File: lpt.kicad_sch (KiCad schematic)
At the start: 20 parts, among them J6 DB25 FEMALE, K1 TE_OJS_5V_10A, Q3 BC857, U2 74HC245, U3 74HC245, U4 LM358EDR2G, U5 ACSL-6400, U7 ACSL-6400

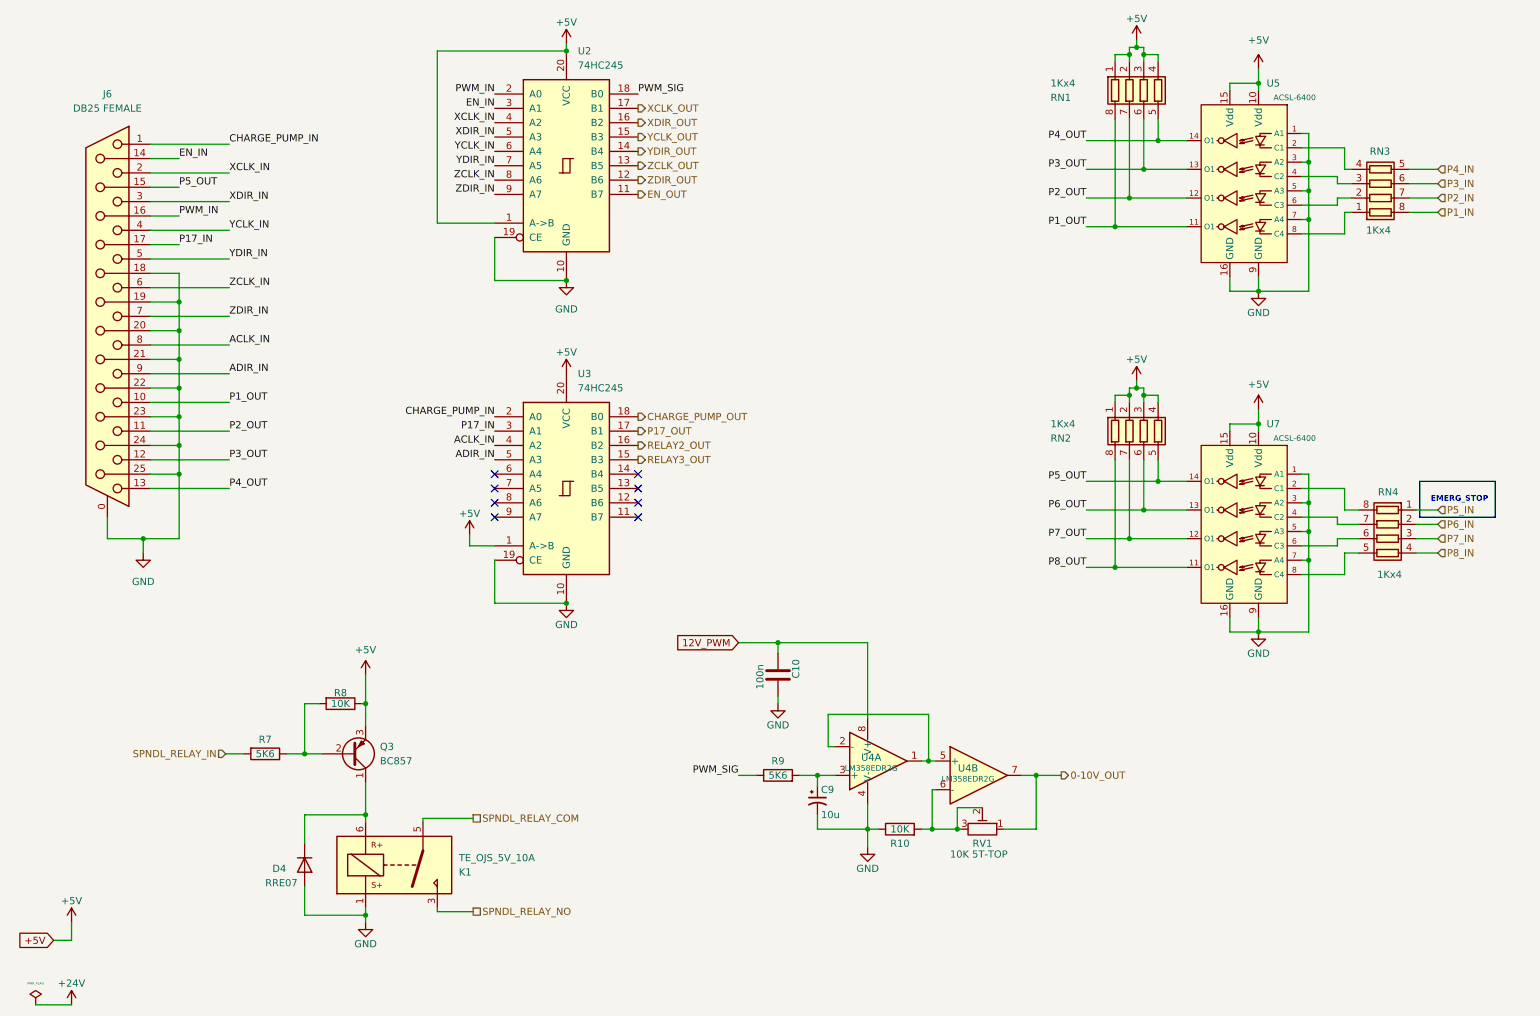
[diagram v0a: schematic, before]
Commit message: Some more decoupling caps and routing optimizations.
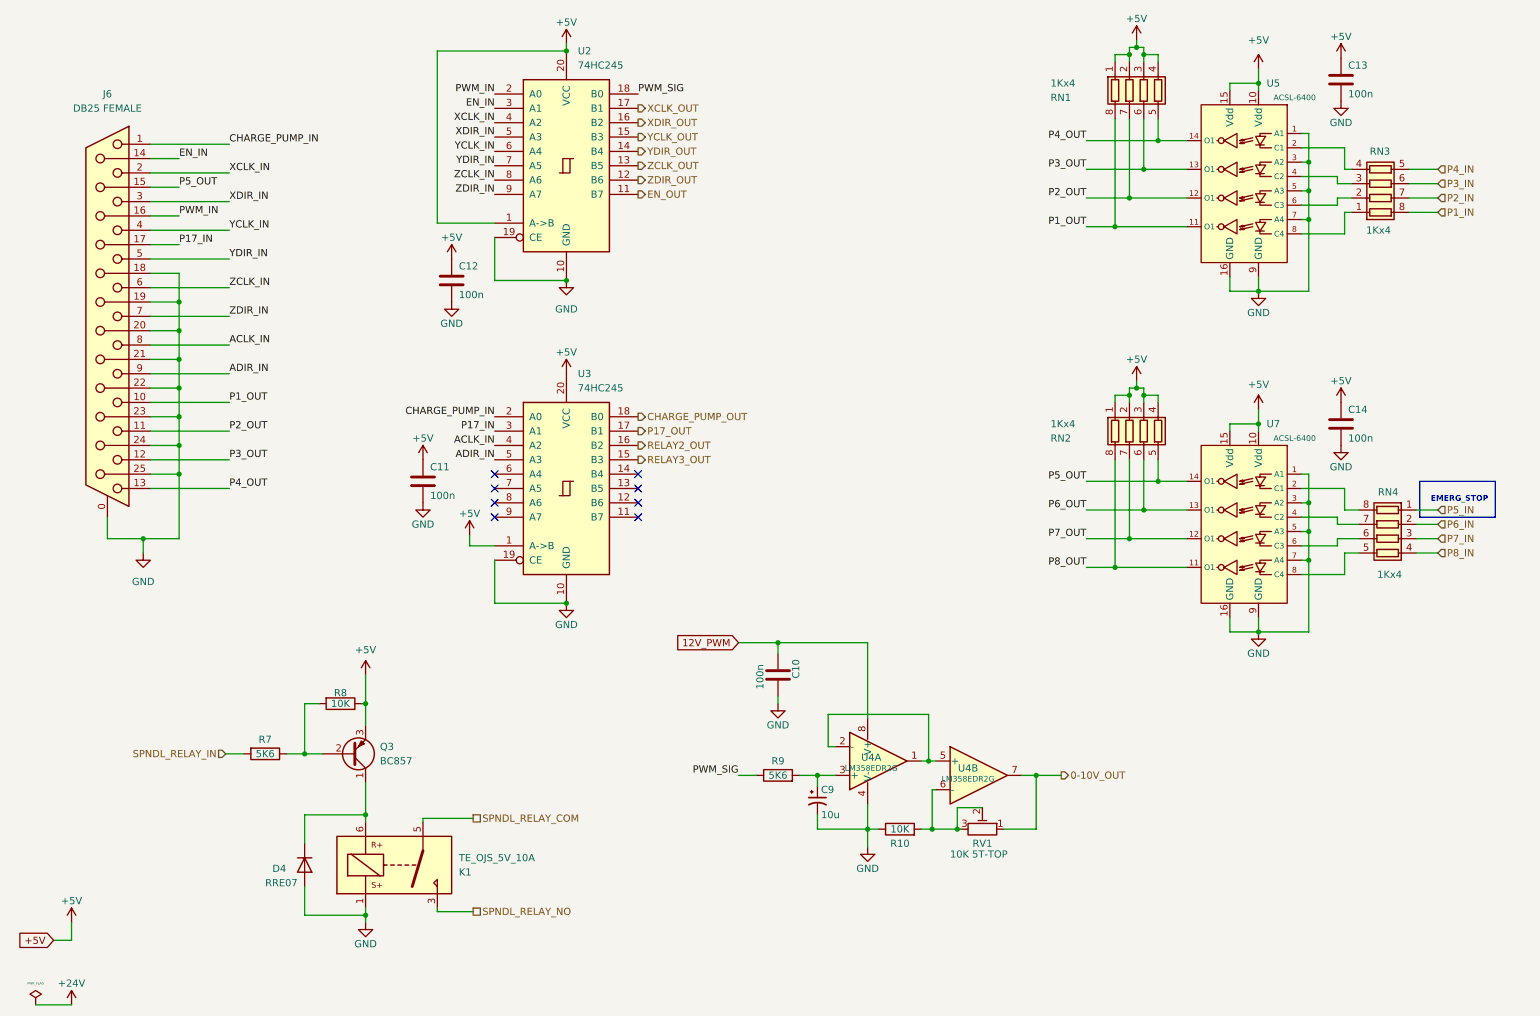
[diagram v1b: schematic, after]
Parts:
- added C11, C12, C13, C14: 100n, Capacitor_SMD:C_0603_1608Metric, symbol Device:C
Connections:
- net +5V: now also C11.1, C12.1, C13.1, C14.1
- net GND: now also C11.2, C12.2, C13.2, C14.2
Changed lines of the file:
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@@
     (effects (font (size 1.27 1.27)) (justify left))
+  )
+  (symbol (lib_id "power:+5V") (at 92.71 58.42 0) (unit 1)
+    (in_bom yes) (on_board yes)
+    (property "Reference" "#PWR041" (id 0) (at 92.71 62.23 0)
+      (effects (font (size 1.27 1.27)) hide)
+    )
+    (property "Value" "+5V" (id 1) (at 92.71 54.61 0))
+    (property "Footprint" "" (id 2) (at 92.71 58.42 0)
+      (effects (font (size 1.27 1.27)) hide)
+    )
+    (property "Datasheet" "" (id 3) (at 92.71 58.42 0)
+      (effects (font (size 1.27 1.27)) hide)
+    )
+    (pin "1")
   )
   (symbol (lib_id "power:PWR_FLAG") (at 19.05 190.5 0) (unit 1)
@@
     (pin "7")
     (pin "8")
+  )
+  (symbol (lib_id "power:GND") (at 92.71 66.04 0) (unit 1)
+    (in_bom yes) (on_board yes)
+    (property "Reference" "#PWR042" (id 0) (at 92.71 72.39 0)
+      (effects (font (size 1.27 1.27)) hide)
+    )
+    (property "Value" "GND" (id 1) (at 92.71 69.85 0))
+    (property "Footprint" "" (id 2) (at 92.71 66.04 0)
+      (effects (font (size 1.27 1.27)) hide)
+    )
+    (property "Datasheet" "" (id 3) (at 92.71 66.04 0)
+      (effects (font (size 1.27 1.27)) hide)
+    )
+    (pin "1")
+  )
+  (symbol (lib_id "power:GND") (at 250.19 91.44 0) (unit 1)
+    (in_bom yes) (on_board yes)
+    (property "Reference" "#PWR046" (id 0) (at 250.19 97.79 0)
+      (effects (font (size 1.27 1.27)) hide)
+    )
+    (property "Value" "GND" (id 1) (at 250.19 95.25 0))
+    (property "Footprint" "" (id 2) (at 250.19 91.44 0)
+      (effects (font (size 1.27 1.27)) hide)
+    )
+    (property "Datasheet" "" (id 3) (at 250.19 91.44 0)
+      (effects (font (size 1.27 1.27)) hide)
+    )
+    (pin "1")
   )
   (symbol (lib_id "power:GND") (at 113.03 119.38 0) (unit 1)
@@
     (pin "9")
   )
+  (symbol (lib_id "Device:C") (at 92.71 62.23 0) (unit 1)
+    (in_bom yes) (on_board yes)
+    (property "Reference" "C12" (id 0) (at 93.98 59.69 0)
+      (effects (font (size 1.27 1.27)) (justify left))
+    )
+    (property "Value" "100n" (id 1) (at 93.98 64.77 0)
+      (effects (font (size 1.27 1.27)) (justify left))
+    )
+    (property "Footprint" "Capacitor_SMD:C_0603_1608Metric" (id 2) (at 93.6752 66.04 0)
+      (effects (font (size 1.27 1.27)) hide)
+    )
+    (property "Datasheet" "~" (id 3) (at 92.71 62.23 0)
+      (effects (font (size 1.27 1.27)) hide)
+    )
+    (pin "1")
+    (pin "2")
+  )
+  (symbol (lib_id "Device:C") (at 250.19 87.63 0) (unit 1)
+    (in_bom yes) (on_board yes)
+    (property "Reference" "C14" (id 0) (at 251.46 85.09 0)
+      (effects (font (size 1.27 1.27)) (justify left))
+    )
+    (property "Value" "100n" (id 1) (at 251.46 90.17 0)
+      (effects (font (size 1.27 1.27)) (justify left))
+    )
+    (property "Footprint" "Capacitor_SMD:C_0603_1608Metric" (id 2) (at 251.1552 91.44 0)
+      (effects (font (size 1.27 1.27)) hide)
+    )
+    (property "Datasheet" "~" (id 3) (at 250.19 87.63 0)
+      (effects (font (size 1.27 1.27)) hide)
+    )
+    (pin "1")
+    (pin "2")
+  )
   (symbol (lib_id "power:+5V") (at 95.885 107.315 0) (unit 1)
     (in_bom yes) (on_board yes)
@@
     )
     (property "Datasheet" "" (id 3) (at 95.885 107.315 0)
+      (effects (font (size 1.27 1.27)) hide)
+    )
+    (pin "1")
+  )
+  (symbol (lib_id "power:+5V") (at 250.19 22.86 0) (unit 1)
+    (in_bom yes) (on_board yes)
+    (property "Reference" "#PWR043" (id 0) (at 250.19 26.67 0)
+      (effects (font (size 1.27 1.27)) hide)
+    )
+    (property "Value" "+5V" (id 1) (at 250.19 19.05 0))
+    (property "Footprint" "" (id 2) (at 250.19 22.86 0)
+      (effects (font (size 1.27 1.27)) hide)
+    )
+    (property "Datasheet" "" (id 3) (at 250.19 22.86 0)
       (effects (font (size 1.27 1.27)) hide)
     )
@@
     )
     (property "Datasheet" "" (id 3) (at 235.585 24.765 0)
+      (effects (font (size 1.27 1.27)) hide)
+    )
+    (pin "1")
+  )
+  (symbol (lib_id "power:GND") (at 250.19 30.48 0) (unit 1)
+    (in_bom yes) (on_board yes)
+    (property "Reference" "#PWR044" (id 0) (at 250.19 36.83 0)
+      (effects (font (size 1.27 1.27)) hide)
+    )
+    (property "Value" "GND" (id 1) (at 250.19 34.29 0))
+    (property "Footprint" "" (id 2) (at 250.19 30.48 0)
+      (effects (font (size 1.27 1.27)) hide)
+    )
+    (property "Datasheet" "" (id 3) (at 250.19 30.48 0)
       (effects (font (size 1.27 1.27)) hide)
     )
@@
     (pin "7")
     (pin "8")
+  )
+  (symbol (lib_id "Device:C") (at 250.19 26.67 0) (unit 1)
+    (in_bom yes) (on_board yes)
+    (property "Reference" "C13" (id 0) (at 251.46 24.13 0)
+      (effects (font (size 1.27 1.27)) (justify left))
+    )
+    (property "Value" "100n" (id 1) (at 251.46 29.21 0)
+      (effects (font (size 1.27 1.27)) (justify left))
+    )
+    (property "Footprint" "Capacitor_SMD:C_0603_1608Metric" (id 2) (at 251.1552 30.48 0)
+      (effects (font (size 1.27 1.27)) hide)
+    )
+    (property "Datasheet" "~" (id 3) (at 250.19 26.67 0)
+      (effects (font (size 1.27 1.27)) hide)
+    )
+    (pin "1")
+    (pin "2")
   )
   (symbol (lib_id "power:+5V") (at 25.4 175.895 0) (unit 1)
@@
     (pin "2")
   )
+  (symbol (lib_id "power:+5V") (at 250.19 83.82 0) (unit 1)
+    (in_bom yes) (on_board yes)
+    (property "Reference" "#PWR045" (id 0) (at 250.19 87.63 0)
+      (effects (font (size 1.27 1.27)) hide)
+    )
+    (property "Value" "+5V" (id 1) (at 250.19 80.01 0))
+    (property "Footprint" "" (id 2) (at 250.19 83.82 0)
+      (effects (font (size 1.27 1.27)) hide)
+    )
+    (property "Datasheet" "" (id 3) (at 250.19 83.82 0)
+      (effects (font (size 1.27 1.27)) hide)
+    )
+    (pin "1")
+  )
   (symbol (lib_id "power:GND") (at 77.47 175.895 0) (unit 1)
     (in_bom yes) (on_board yes)
@@
     (pin "2")
   )
+  (symbol (lib_id "power:+5V") (at 87.63 93.98 0) (unit 1)
+    (in_bom yes) (on_board yes)
+    (property "Reference" "#PWR039" (id 0) (at 87.63 97.79 0)
+      (effects (font (size 1.27 1.27)) hide)
+    )
+    (property "Value" "+5V" (id 1) (at 87.63 90.17 0))
+    (property "Footprint" "" (id 2) (at 87.63 93.98 0)
+      (effects (font (size 1.27 1.27)) hide)
+    )
+    (property "Datasheet" "" (id 3) (at 87.63 93.98 0)
+      (effects (font (size 1.27 1.27)) hide)
+    )
+    (pin "1")
+  )
   (symbol (lib_id "power:GND") (at 235.585 64.135 0) (unit 1)
     (in_bom yes) (on_board yes)
@@
     (pin "1")
   )
+  (symbol (lib_id "power:GND") (at 87.63 101.6 0) (unit 1)
+    (in_bom yes) (on_board yes)
+    (property "Reference" "#PWR040" (id 0) (at 87.63 107.95 0)
+      (effects (font (size 1.27 1.27)) hide)
+    )
+    (property "Value" "GND" (id 1) (at 87.63 105.41 0))
+    (property "Footprint" "" (id 2) (at 87.63 101.6 0)
+      (effects (font (size 1.27 1.27)) hide)
+    )
+    (property "Datasheet" "" (id 3) (at 87.63 101.6 0)
+      (effects (font (size 1.27 1.27)) hide)
+    )
+    (pin "1")
+  )
   (symbol (lib_id "power:GND") (at 235.585 124.46 0) (unit 1)
     (in_bom yes) (on_board yes)
@@
     (pin "1")
   )
+  (symbol (lib_id "Device:C") (at 87.63 97.79 0) (unit 1)
+    (in_bom yes) (on_board yes)
+    (property "Reference" "C11" (id 0) (at 88.9 95.25 0)
+      (effects (font (size 1.27 1.27)) (justify left))
+    )
+    (property "Value" "100n" (id 1) (at 88.9 100.33 0)
+      (effects (font (size 1.27 1.27)) (justify left))
+    )
+    (property "Footprint" "Capacitor_SMD:C_0603_1608Metric" (id 2) (at 88.5952 101.6 0)
+      (effects (font (size 1.27 1.27)) hide)
+    )
+    (property "Datasheet" "~" (id 3) (at 87.63 97.79 0)
+      (effects (font (size 1.27 1.27)) hide)
+    )
+    (pin "1")
+    (pin "2")
+  )
   (symbol (lib_id "Relay:ADW11") (at 82.55 165.735 0) (mirror x) (unit 1)

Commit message: Lots of changes and errors fixed. Updated vanity images.
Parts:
- added R11: 100, Resistor_SMD:R_0603_1608Metric, symbol Device:R
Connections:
- net ACLK_IN is gone; now on net P8_IN: J6.8, U3.4 (A2)
- net CHARGE_PUMP_IN is gone; now on net P1_IN: J6.1, U3.2 (A0)
- net CHARGE_PUMP_OUT is gone; now on net P1_OUT: U3.18 (B0)
- net EN_OUT is gone; now on net P7_OUT: U2.11 (B7)
- net RELAY2_OUT is gone; now on net P8_OUT: U3.16 (B2)
- net XCLK_IN is gone; now on net P2_IN: J6.2, U2.4 (A2)
- net XDIR_IN is gone; now on net P3_IN: J6.3, U2.5 (A3)
- net XDIR_OUT is gone; now on net P2_OUT: U2.16 (B2)
- net YCLK_IN is gone; now on net P4_IN: J6.4, U2.6 (A4)
- net YCLK_OUT is gone; now on net P3_OUT: U2.15 (B3)
- net YDIR_IN is gone; now on net P5_IN: J6.5, U2.7 (A5)
- net YDIR_OUT is gone; now on net P4_OUT: U2.14 (B4)
- net ZCLK_IN is gone; now on net P6_IN: J6.6, U2.8 (A6)
- net ZCLK_OUT is gone; now on net P5_OUT: U2.13 (B5)
- net ZDIR_IN is gone; now on net P7_IN: J6.7, U2.9 (A7)
- net ZDIR_OUT is gone; now on net P6_OUT: U2.12 (B6)
- net 12V_PWM: now also R11.1; no longer C10.1, U4.8 (V+)
- net P1_IN: no longer RN3.8 (R1.2)
- net P1_OUT: no longer J6.10, RN1.8 (R1.2), U5.11 (O1)
- net P2_IN: no longer RN3.7 (R2.2)
- net P2_OUT: no longer J6.11, RN1.7 (R2.2), U5.12 (O1)
- net P3_IN: no longer RN3.6 (R3.2)
- net P3_OUT: no longer J6.12, RN1.6 (R3.2), U5.13 (O1)
- net P4_IN: no longer RN3.5 (R4.2)
- net P4_OUT: no longer J6.13, RN1.5 (R4.2), U5.14 (O1)
- net P5_IN: no longer RN4.1 (R1.1)
- net P5_OUT: no longer J6.15 (P15), RN2.5 (R4.2), U7.14 (O1)
- net P6_IN: no longer RN4.2 (R2.1)
- net P6_OUT: no longer RN2.6 (R3.2), U7.13 (O1)
- net P7_IN: no longer RN4.3 (R3.1)
- net P7_OUT: no longer RN2.7 (R2.2), U7.12 (O1)
- net P8_IN: no longer RN4.4 (R4.1)
- net P8_OUT: no longer RN2.8 (R1.2), U7.11 (O1)
- net PWM_IN: now also R9.2; no longer J6.16 (P16), U2.2 (A0)
- net at C9.1, U4.3 (+): now also R9.1; no longer R9.2
- net ADIR_IN renamed P9_IN
- net EN_IN renamed P14_IN
- net PWM_SIG renamed P16_OUT
- net P16_OUT: no longer R9.1
- net RELAY3_OUT renamed P9_OUT
- net XCLK_OUT renamed P14_OUT
- new net: C10.1, R11.2, U4.8 (V+)
- new net: RN2.6 (R3.2), U7.13 (O1)
- new net: RN2.7 (R2.2), U7.12 (O1)
- new net: RN2.8 (R1.2), U7.11 (O1)
- new net P10_IN: RN3.8 (R1.2)
- new net P10_OUT: J6.10, RN1.8 (R1.2), U5.11 (O1)
- new net P11_IN: RN3.7 (R2.2)
- new net P11_OUT: J6.11, RN1.7 (R2.2), U5.12 (O1)
- new net P12_IN: RN3.6 (R3.2)
- new net P12_OUT: J6.12, RN1.6 (R3.2), U5.13 (O1)
- new net P13_IN: RN3.5 (R4.2)
- new net P13_OUT: J6.13, RN1.5 (R4.2), U5.14 (O1)
- new net P15_IN: RN4.1 (R1.1)
- new net P15_OUT: J6.15 (P15), RN2.5 (R4.2), U7.14 (O1)
- new net P16_IN: J6.16 (P16), U2.2 (A0)
- no-connect marks 8 -> 12
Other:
- moved on the sheet: C10, C11, C12, C9, D4, K1, Q3, R10, R7, R8, R9, RN4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

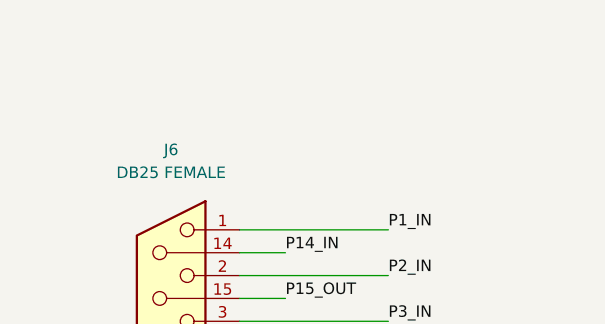
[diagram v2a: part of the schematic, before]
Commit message: Probe connectors wired wrong. Improved 5V buck reg layout.
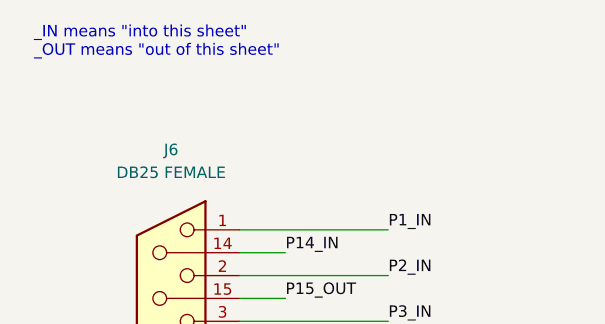
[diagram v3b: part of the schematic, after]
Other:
- note added: "_IN means "into this sheet" _OUT means "out of this sheet""
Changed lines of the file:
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@@
     (stroke (width 0) (type default) (color 0 0 0 0))
+  )
+  (text "_IN means \"into this sheet\"\n_OUT means \"out of this sheet\""
+    (at 16.51 19.05 0)
+    (effects (font (size 1.27 1.27)) (justify left bottom))
   )
   (text "EMERG_STOP" (at 266.065 101.6 0)
